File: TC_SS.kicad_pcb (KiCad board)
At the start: 2 copper layers, 106.7 x 124.5 mm, 41 parts, among them Q1 IPW60R099P6XKSA1, Q2 IPW60R099P6XKSA1, Q3 IPW60R099P6XKSA1, Q4 IPW60R099P6XKSA1, U1 IR2184, U2 IR2184, U3 SN74LVC1G14DBV, U4 SN74LVC1G14DBV, U5 NE555D

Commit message: Update Power PCB
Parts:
- added C12: 100n?, Capacitor_SMD:C_2220_5650Metric, F.Cu at (138.5, 121.5)
- added C13: 100n?, Capacitor_SMD:C_2220_5650Metric, F.Cu at (138.5, 114.5)
- added C14: 100n?, Capacitor_SMD:C_2220_5650Metric, F.Cu at (138.5, 107.0)
- added C15: 100n?, Capacitor_SMD:C_2220_5650Metric, F.Cu at (138.5, 99.5)
- added C16: 100n?, Capacitor_SMD:C_2220_5650Metric, F.Cu at (187.5, 121.0)
- added C17: 100n?, Capacitor_SMD:C_2220_5650Metric, F.Cu at (187.5, 114.0)
- added C18: 100n?, Capacitor_SMD:C_2220_5650Metric, F.Cu at (195.0, 109.5)
- added C19: 100n?, Capacitor_SMD:C_2220_5650Metric, F.Cu at (202.0, 109.5)
- added C20: 100n, Capacitor_SMD:C_2220_5650Metric, F.Cu at (177.9, 134.6)
- added C21: 100n, Capacitor_SMD:C_2220_5650Metric, F.Cu at (177.9, 140.5)
- C1, C10, C11: value 100n? -> 100n; footprint Capacitor_SMD:C_2220_5750Metric -> Capacitor_SMD:C_2220_5650Metric
- C3, C4, C5, C6: footprint Capacitor_THT:C_Radial_D8.0mm_H11.5mm_P3.50mm -> Capacitor_THT:CP_Radial_D35.0mm_P10.00mm_SnapIn
- moved FL1 175.0 mm to (17.7, 103.5)
- moved D2 132.2 mm to (48.1, 106.7)
- moved C4 120.1 mm to (28.0, 71.0)
- moved C5 108.7 mm to (28.0, 33.0)
- moved C3 78.6 mm to (67.1, 70.5)
- moved C6 67.5 mm to (67.0, 32.0)
- moved D11 65.2 mm to (166.0, 58.5), turned to 180 degrees
- moved D1 63.6 mm to (129.5, 126.0), turned to 180 degrees
- moved D3 62.6 mm to (210.5, 129.0), turned to 180 degrees
- moved R6 56.1 mm to (208.0, 138.0), turned to -90 degrees
- moved D10 52.7 mm to (152.2, 64.1)
- moved D8 52.7 mm to (152.2, 53.0)
- moved D9 52.7 mm to (152.2, 58.5)
- moved C2 51.6 mm to (132.5, 129.5), turned to 180 degrees
- moved D6 51.6 mm to (202.5, 138.0), turned to 180 degrees
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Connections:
- net Net-(D4-A) renamed /HS1_G
- net Net-(D5-A) renamed /LS1_G
- net Net-(Q1-S) renamed /HB1
- net Net-(Q3-D) renamed /HB2
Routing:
- net /HB1: track 41.8 -> 0.00 mm
- net Net-(D4-K): track 24.3 -> 0.00 mm
- net /HB2: track 27.8 -> 4.50 mm
- net Net-(D5-K): track 22.5 -> 0.00 mm
- net GND: track 21.8 -> 4.77 mm, vias 0 -> 80
- net /HS1_G: track 13.4 -> 0.00 mm
- net /HS2_G: track 3.56 -> 11.5 mm
- net /LS1_G: track 7.64 -> 0.00 mm
- net Net-(D1-K): track 0.00 -> 7.04 mm
- net Net-(D1-A): track 0.00 -> 6.75 mm
- net Net-(D3-A): track 0.00 -> 6.13 mm
- net Net-(D3-K): track 0.00 -> 5.18 mm
- net Net-(U1-VS): track 0.00 -> 4.93 mm
- net Net-(U2-VS): track 0.00 -> 4.54 mm
- net /LS2_G: track 3.72 -> 7.91 mm
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- added copper zone on F.Cu, net /HB1
- added copper zone on F.Cu, net /HB2
- added copper zone on F.Cu, net /HS1_G
- added copper zone on F.Cu, net /LS1_G
- added copper zone on B.Cu, net GND
- added copper zone on F.Cu, net Net-(C1-Pad1)
- added copper zone on F.Cu, net Net-(D4-K)
- added copper zone on F.Cu, net Net-(D5-K)
- added copper zone on F.Cu, net VDC

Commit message: Do power PCB layout
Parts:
- moved R8 67.1 mm to (151.5, 130.0)
- moved C14 17.7 mm to (156.0, 109.5), turned to -90 degrees
- moved C15 14.1 mm to (148.5, 109.5), turned to -90 degrees
- moved R6 9.01 mm to (200.5, 143.0), turned to 90 degrees
- moved C18 7.52 mm to (202.5, 110.0), turned to -90 degrees
- moved C19 6.52 mm to (195.5, 110.0), turned to -90 degrees
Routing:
- net Net-(D7-K): track 13.1 -> 0.00 mm
- net /HS2_G: track 11.5 -> 0.00 mm
- net Net-(D6-K): track 8.49 -> 0.00 mm
- net /LS2_G: track 7.91 -> 0.00 mm
- net Net-(D1-K): track 7.04 -> 0.00 mm
- net Net-(D1-A): track 6.75 -> 0.00 mm
- net Net-(D3-A): track 6.13 -> 0.00 mm
- net Net-(D3-K): track 5.18 -> 0.00 mm
- net Net-(U1-VS): track 4.93 -> 0.00 mm
- net GND: track 4.77 -> 0.00 mm, vias 80 -> 82
- net Net-(U2-VS): track 4.54 -> 0.00 mm
- net /HB2: track 4.50 -> 0.00 mm
- added copper zone on F.Cu, net /HS2_G
- added copper zone on F.Cu, net /LS2_G
- added copper zone on F.Cu, net Net-(D1-A)
- added copper zone on F.Cu, net Net-(D1-K)
- added copper zone on F.Cu, net Net-(D3-A)
- added copper zone on F.Cu, net Net-(D3-K)
- added copper zone on F.Cu, net Net-(D6-K)
- added copper zone on F.Cu, net Net-(D7-K)
- added copper zone on F.Cu, net Net-(U1-VS)
- added copper zone on F.Cu, net Net-(U2-VS)
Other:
- board size 106.7 x 124.5 mm -> 93.2 x 51 mm

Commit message: Update schematic
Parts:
- removed C3, C4, C5, C6: 330u, Capacitor_THT:CP_Radial_D35.0mm_P10.00mm_SnapIn
- removed C8, C9: C, Capacitor_SMD:C_0805_2012Metric_Pad1.18x1.45mm_HandSolder
- removed D10, D11, D8, D9: 1n4148, Diode_SMD:D_SMB
- removed D2: D_Bridge_+-AA, Diode_THT:Diode_Bridge_Vishay_KBPC6
- removed FL1: Filter_EMI_CommonMode, Inductor_THT:L_CommonMode_PulseElectronics_PH9455x155NL_1
- removed U3, U4: SN74LVC1G14DBV, Package_TO_SOT_SMD:SOT-23-5
- removed U5: NE555D, Package_SO:SOIC-8_3.9x4.9mm_P1.27mm
- C12, C13, C14, C15, C16, C17, C18, C19: value 100n? -> 100n

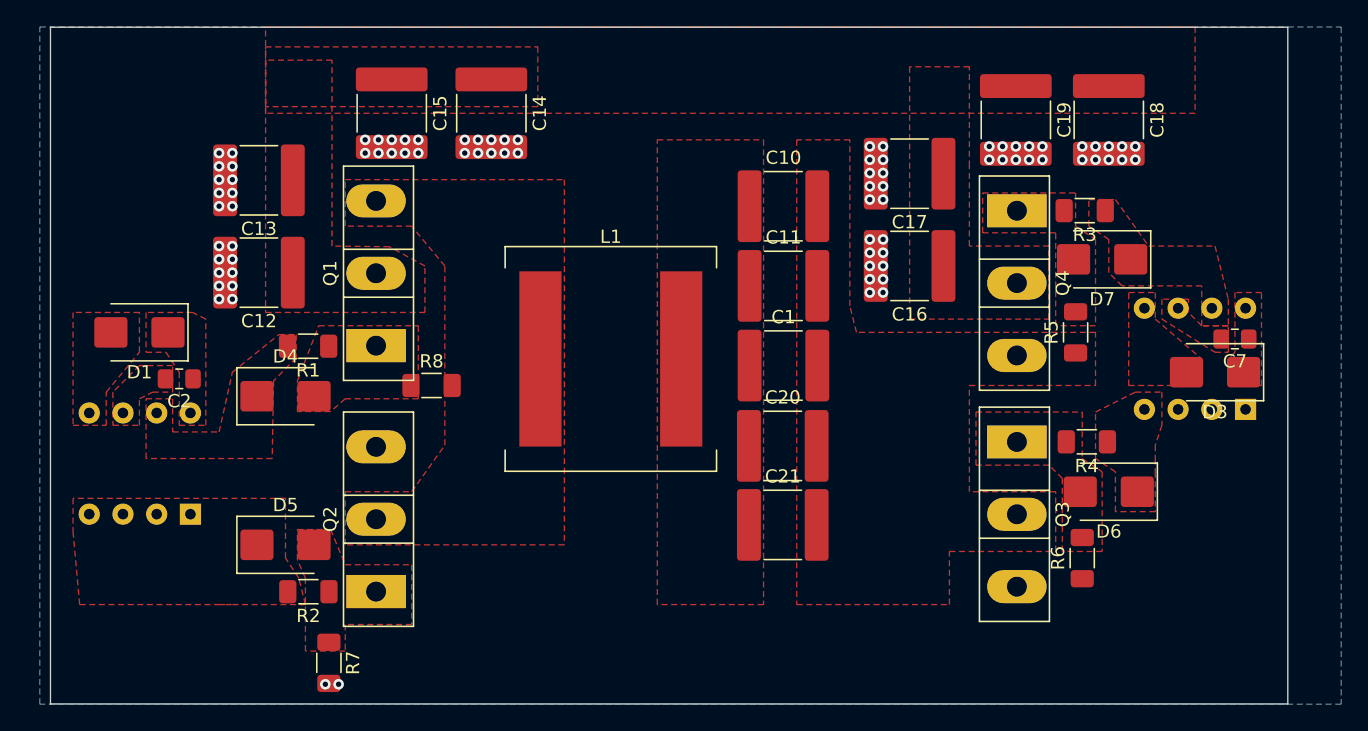
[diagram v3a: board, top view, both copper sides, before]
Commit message: Swap gate driver for Adum4221-1
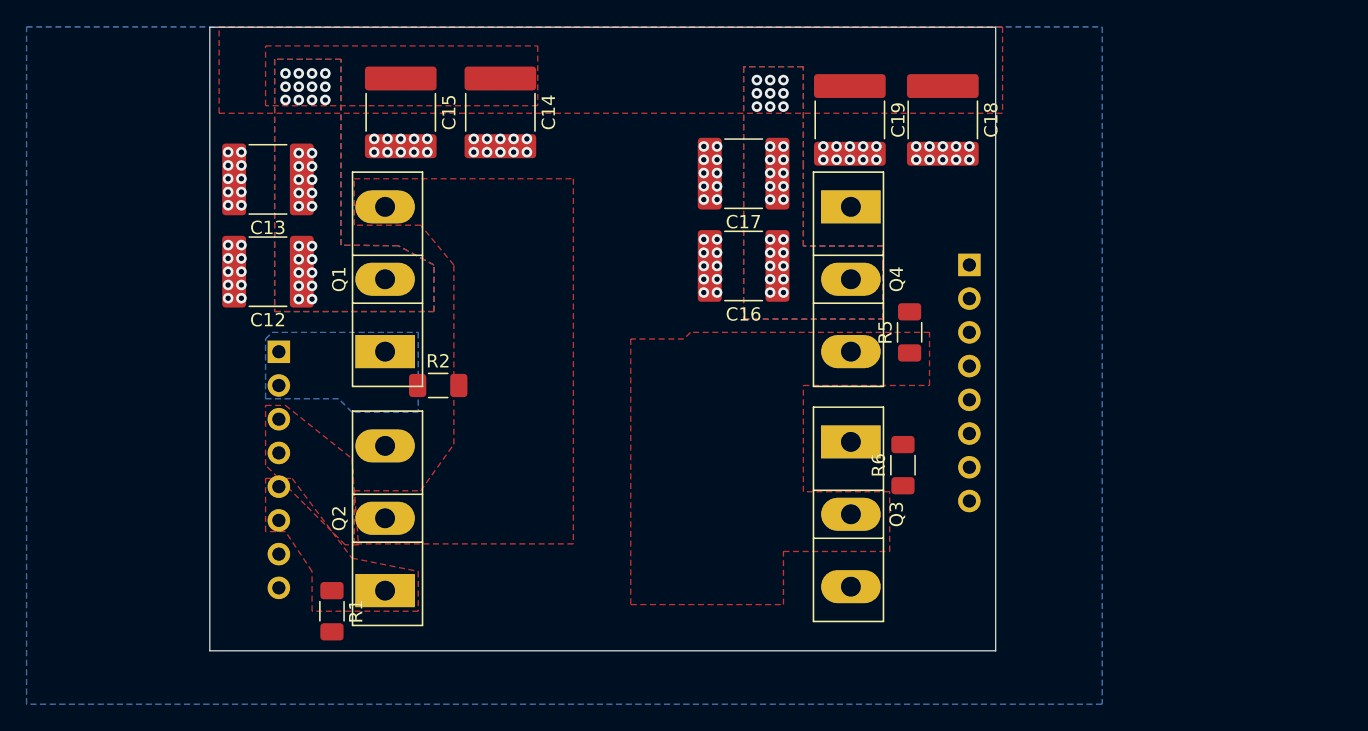
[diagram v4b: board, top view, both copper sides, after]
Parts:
- removed C1, C10, C11, C20, C21: 100n, Capacitor_SMD:C_2220_5650Metric
- removed C2, C7: 100n, Capacitor_SMD:C_0805_2012Metric_Pad1.18x1.45mm_HandSolder
- removed D1, D3: STTH2R06, Diode_SMD:D_SMB
- removed D4, D5, D6, D7: 1n4148, Diode_SMD:D_SMB
- removed L1: ?, Inductor_SMD:L_Coilcraft_XAL1510-472
- removed R3, R4: 22, Resistor_SMD:R_1206_3216Metric_Pad1.30x1.75mm_HandSolder
- removed R7, R8: 10k, Resistor_SMD:R_1206_3216Metric_Pad1.30x1.75mm_HandSolder
- removed U1, U2: IR2184, Package_DIP:DIP-8_W7.62mm_Socket
- added J1: Conn_01x08_Pin, Connector_PinHeader_2.54mm:PinHeader_1x08_P2.54mm_Vertical, B.Cu at (140.0, 127.5)
- added J2: Conn_01x08_Pin, Connector_PinHeader_2.54mm:PinHeader_1x08_P2.54mm_Vertical, B.Cu at (192.0, 120.9)
- R1, R2: value 22 -> 10k
- moved R1 20.0 mm to (144.0, 147.0), turned to -90 degrees
- moved R2 18.4 mm to (152.0, 130.0), turned to 0 degrees
- moved R6 15.2 mm to (187.0, 136.0)
- moved Q4 12.5 mm to (183.1, 116.5)
- moved C16 12.5 mm to (175.0, 121.0)
- moved C17 12.5 mm to (175.0, 114.0)
- moved C18 12.5 mm to (190.0, 110.0)
- moved C19 12.5 mm to (183.0, 110.0)
- moved Q3 12.5 mm to (183.1, 134.2)
- moved R5 12.5 mm to (187.5, 126.0)
- moved Q1 0.82 mm to (148.0, 127.5)
- moved Q2 0.68 mm to (148.0, 145.4)
- moved C12 0.68 mm to (139.2, 121.4)
- moved C13 0.68 mm to (139.2, 114.5)
- moved C14 0.68 mm to (156.7, 109.4)
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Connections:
- net /HS2_G renamed Net-(J2-Pin_7)
- net /LS2_G renamed Net-(J2-Pin_3)
- R1 pad 1: /HS1_G -> /LS1_G
- R1 pad 2: Net-(D4-K) -> GND
- R2 pad 1: /LS1_G -> /HS1_G
- R2 pad 2: Net-(D5-K) -> /HB1
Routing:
- net VDC: vias 0 -> 61
- net GND: vias 82 -> 80
- added copper zone on B.Cu, net /HS1_G
- added copper zone on B.Cu, net VDC
- removed copper zone on F.Cu, net /HS1_G
- removed copper zone on F.Cu, net Net-(C1-Pad1)
- removed copper zone on F.Cu, net Net-(D1-A)
- removed copper zone on F.Cu, net Net-(D1-K)
- removed copper zone on F.Cu, net Net-(D3-A)
- removed copper zone on F.Cu, net Net-(D3-K)
- removed copper zone on F.Cu, net Net-(D4-K)
- removed copper zone on F.Cu, net Net-(D5-K)
- removed copper zone on F.Cu, net Net-(D6-K)
- removed copper zone on F.Cu, net Net-(D7-K)
- removed copper zone on F.Cu, net Net-(J2-Pin_3)
- removed copper zone on F.Cu, net Net-(J2-Pin_7)
- removed copper zone on F.Cu, net Net-(U1-VS)
- removed copper zone on F.Cu, net Net-(U2-VS)
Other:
- board size 93.2 x 51 mm -> 59.2 x 47 mm

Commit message: Update basically everything
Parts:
- removed J2: Conn_01x08_Pin, Connector_PinHeader_2.54mm:PinHeader_1x08_P2.54mm_Vertical
- added C1: 1u, Capacitor_SMD:C_0805_2012Metric, F.Cu at (202.7, 120.7)
- added C2: 1u, Capacitor_SMD:C_0805_2012Metric, F.Cu at (202.7, 117.7)
- added C3: 100n, Capacitor_SMD:C_2220_5650Metric, F.Cu at (114.5, 133.1)
- added C4: 1u, Capacitor_SMD:C_0805_2012Metric, F.Cu at (112.5, 107.1)
- added C5: 1u, Capacitor_SMD:C_0805_2012Metric, F.Cu at (112.5, 110.1)
- added C6: 1u, Capacitor_SMD:C_0805_2012Metric, F.Cu at (112.5, 113.1)
- added C7: 1u, Capacitor_SMD:C_0805_2012Metric, F.Cu at (112.5, 116.1)
- added C8: 1u, Capacitor_SMD:C_0805_2012Metric, F.Cu at (112.5, 119.2)
- added C9: 1u, Capacitor_SMD:C_0805_2012Metric, F.Cu at (112.5, 122.2)
- added D1: D, PCM_Diode_SMD_AKL:D_PowerDI-123, F.Cu at (188.5, 136.0)
- added D2: 1N4148WT, Diode_SMD:D_SOD-523, F.Cu at (116.5, 106.8)
- added D3: 1N4148WT, Diode_SMD:D_SOD-523, F.Cu at (116.5, 109.3)
- added D4: D, PCM_Diode_SMD_AKL:D_PowerDI-123, F.Cu at (211.5, 138.4)
- added D5: D, PCM_Diode_SMD_AKL:D_PowerDI-123, F.Cu at (211.5, 142.7)
- added D6: D, PCM_Diode_SMD_AKL:D_PowerDI-123, F.Cu at (211.5, 147.0)
- added IC1: ADUM4221-1ARIZ, SamacSys_Parts:SOIC127P1030X264-16N, F.Cu at (137.0, 134.0)
- added IC2: ADUM4221-1ARIZ, SamacSys_Parts:SOIC127P1030X264-16N, F.Cu at (195.5, 127.5)
- added PS1: RKZ-1215S_H, symbol:RKZ1215SH, B.Cu at (125.0, 108.3)
- added PS2: RKZ-1215S_H, symbol:RKZ1215SH, B.Cu at (123.2, 134.2)
- added PS3: RKZ-1215S_H, symbol:RKZ1215SH, B.Cu at (195.2, 153.2)
- added PS4: RKZ-1215S_H, symbol:RKZ1215SH, B.Cu at (213.5, 104.5)
- added R10: 100, Resistor_SMD:R_0805_2012Metric, F.Cu at (117.1, 138.1)
- added R11: 4.7, Resistor_SMD:R_0805_2012Metric, F.Cu at (117.1, 141.0)
- added R3: 10k, Resistor_SMD:R_0805_2012Metric, F.Cu at (207.1, 132.3)
- added R4: 10k, Resistor_SMD:R_0805_2012Metric, F.Cu at (207.1, 129.4)
- added R7: 22, Resistor_SMD:R_0805_2012Metric, F.Cu at (187.5, 133.5)
- added R8: 22, Resistor_SMD:R_0805_2012Metric, F.Cu at (207.1, 117.6)
- added R9: 4.7, Resistor_SMD:R_0805_2012Metric, F.Cu at (207.1, 114.6)
- added U1: LM7805_TO220, Package_TO_SOT_THT:TO-220-3_Vertical, F.Cu at (113.5, 127.6)
- J1: value Conn_01x08_Pin -> 12V_In; footprint Connector_PinHeader_2.54mm:PinHeader_1x08_P2.54mm_Vertical -> Connector_PinHeader_2.54mm:PinHeader_1x02_P2.54mm_Vertical; moved to F.Cu
- R1, R2, R5, R6: footprint Resistor_SMD:R_1206_3216Metric_Pad1.30x1.75mm_HandSolder -> Resistor_SMD:R_0805_2012Metric
- moved J1 29.7 mm to (112.6, 138.9), turned to 0 degrees
- moved R5 19.6 mm to (207.1, 126.4), turned to 180 degrees
- moved R6 17.0 mm to (202.5, 143.0), turned to 180 degrees
- moved C12 2.81 mm to (136.4, 121.4)
- moved C13 2.81 mm to (136.4, 114.5)
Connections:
- J1 pad 1: /HS1_G -> GND
- J1 pad 2: /HS1_G -> +12V
- Q1 pad 3: /HB1 -> HB1
- Q2 pad 2: /HB1 -> HB1
- Q3 pad 1: Net-(J2-Pin_3) -> Net-(D1-A)
- Q3 pad 2: /HB2 -> HB2
- Q4 pad 1: Net-(J2-Pin_7) -> Net-(D4-A)
- Q4 pad 3: /HB2 -> HB2
- R2 pad 2: /HB1 -> HB1
- R5 pad 1: /HB2 -> Net-(D6-A)
- R5 pad 2: Net-(J2-Pin_7) -> /HS1_G
- R6 pad 1: GND -> Net-(D5-A)
- R6 pad 2: Net-(J2-Pin_3) -> /LS1_G
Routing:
- net GND: vias 80 -> 81
- added copper zone on F.Cu, net HB1
- added copper zone on F.Cu, net HB2
- removed copper zone on F.Cu, net /HB1
- removed copper zone on F.Cu, net /HB2
- removed copper zone on F.Cu, net /LS1_G
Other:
- board size 59.2 x 47 mm -> 106.7 x 58 mm

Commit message: Almost ready to produce
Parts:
- added C10: 10u, Capacitor_SMD:C_0805_2012Metric, F.Cu at (115.4, 108.1)
- added C11: 1u, Capacitor_SMD:C_0805_2012Metric, F.Cu at (119.4, 108.1)
- added C20: 1u, Capacitor_SMD:C_0805_2012Metric, F.Cu at (137.2, 147.5)
- added C21: 1u, Capacitor_SMD:C_0805_2012Metric, F.Cu at (133.8, 147.5)
- added C22: 1u, Capacitor_SMD:C_0805_2012Metric, B.Cu at (136.8, 132.5)
- added C23: 1u, Capacitor_SMD:C_0805_2012Metric, B.Cu at (133.2, 132.5)
- added C24: 100n, Capacitor_SMD:C_0805_2012Metric, F.Cu at (137.0, 145.5)
- added C25: 100n, Capacitor_SMD:C_0805_2012Metric, F.Cu at (133.8, 145.5)
- added C26: 100n, Capacitor_SMD:C_0805_2012Metric, B.Cu at (133.2, 134.5)
- added C27: 100n, Capacitor_SMD:C_0805_2012Metric, B.Cu at (136.8, 134.5)
- added C28: 1u, Capacitor_SMD:C_0805_2012Metric, F.Cu at (189.6, 159.7)
- added C29: 1u, Capacitor_SMD:C_0805_2012Metric, F.Cu at (189.6, 162.8)
- added C30: 1u, Capacitor_SMD:C_0805_2012Metric, F.Cu at (195.0, 116.0)
- added C31: 1u, Capacitor_SMD:C_0805_2012Metric, F.Cu at (194.1, 153.7)
- added C32: 1u, Capacitor_SMD:C_0805_2012Metric, F.Cu at (194.1, 156.7)
- added C33: 1u, Capacitor_SMD:C_0805_2012Metric, F.Cu at (194.1, 159.7)
- added C34: 100n, Capacitor_SMD:C_0805_2012Metric, F.Cu at (194.1, 162.8)
- added C35: 100n, Capacitor_SMD:C_0805_2012Metric, F.Cu at (198.5, 150.7)
- added C36: 1u, Capacitor_SMD:C_0805_2012Metric, F.Cu at (198.5, 153.7)
- added C37: 1u, Capacitor_SMD:C_0805_2012Metric, F.Cu at (123.2, 147.5)
- added C38: 1u, Capacitor_SMD:C_0805_2012Metric, F.Cu at (123.0, 127.5)
- added C39: 1u, Capacitor_SMD:C_0805_2012Metric, F.Cu at (198.5, 162.8)
- added H1: MountingHole_Pad, MountingHole:MountingHole_3.2mm_M3_Pad_Via, F.Cu at (114.8, 157.5)
- added H2: MountingHole_Pad, MountingHole:MountingHole_3.2mm_M3_Pad_Via, F.Cu at (114.2, 117.0)
- added H3: MountingHole_Pad, MountingHole:MountingHole_3.2mm_M3_Pad_Via, F.Cu at (204.8, 105.2)
- added H4: MountingHole_Pad, MountingHole:MountingHole_3.2mm_M3_Pad_Via, F.Cu at (121.8, 157.5)
- added J2: Conn_Coaxial, Connector_Coaxial:SMA_Samtec_SMA-J-P-X-ST-EM1_EdgeMount, F.Cu at (85.4, 109.7)
- added J3: Conn_Coaxial, Connector_Coaxial:SMA_Samtec_SMA-J-P-X-ST-EM1_EdgeMount, F.Cu at (112.7, 133.2)
- added J4: Conn_Coaxial, Connector_Coaxial:SMA_Samtec_SMA-J-P-X-ST-EM1_EdgeMount, F.Cu at (112.7, 142.8)
- added J5: Conn_Coaxial, Connector_Coaxial:SMA_Samtec_SMA-J-P-X-ST-EM1_EdgeMount, F.Cu at (221.8, 124.8)
- added J6: Conn_Coaxial, Connector_Coaxial:SMA_Samtec_SMA-J-P-X-ST-EM1_EdgeMount, F.Cu at (221.6, 139.2)
- added TP1: TestPoint, TestPoint:TestPoint_Loop_D3.50mm_Drill1.4mm_Beaded, F.Cu at (83.3, 119.7)
- added TP2: TestPoint, TestPoint:TestPoint_Loop_D3.50mm_Drill1.4mm_Beaded, F.Cu at (102.8, 119.4)
- added U2: 74HC14, SamacSys_Parts:SOIC127P600X175-14N, F.Cu at (93.0, 109.7)
- added U3: LM7812_TO220, Package_TO_SOT_THT:TO-220-3_Vertical, F.Cu at (114.8, 104.1)
- C4: value 1u -> 10u
- C8, C9: moved to B.Cu
- D1, D4, D5, D6: value D -> DFLS120L-7
- J1: value 12V_In -> 15V_In
- R5, R6: value 10k -> 22
- moved C8 89.3 mm to (201.0, 130.8), turned to 180 degrees
- moved C9 88.3 mm to (200.8, 124.5), turned to 180 degrees
- moved R11 88.2 mm to (204.5, 129.2), turned to 90 degrees
- moved R9 83.5 mm to (127.2, 139.0), turned to -90 degrees
- moved D6 70.5 mm to (143.0, 130.2)
- moved D5 68.0 mm to (143.5, 143.5)
- moved R5 63.6 mm to (143.5, 127.8), turned to 0 degrees
- moved R6 58.8 mm to (143.8, 145.8), turned to 0 degrees
- moved PS3 36.3 mm to (209.7, 120.0)
- moved PS4 33.9 mm to (209.8, 138.2)
- moved J1 27.6 mm to (111.9, 111.3), turned to 180 degrees
- moved D3 27.4 mm to (89.8, 115.4), turned to 180 degrees
- moved U1 27.0 mm to (127.0, 104.2)
- moved R10 26.9 mm to (96.8, 120.4), turned to 90 degrees
- moved C3 26.2 mm to (92.1, 119.4)
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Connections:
- D3 pad 2: Net-(D3-A) -> GND
- D5 pad 1: /LS1_G -> Net-(D5-K)
- D5 pad 2: Net-(D5-A) -> /LS1_G
- D6 pad 1: /HS1_G -> Net-(D6-K)
- D6 pad 2: Net-(D6-A) -> /HS1_G
- IC1 pad 1: PWM -> Net-(IC1-PWM)
- IC1 pad 10: Net-(D5-A) -> Net-(D5-K)
- IC1 pad 15: Net-(D6-A) -> Net-(D6-K)
- IC1 pad 5: unconnected-(IC1-DISABLE-Pad5) -> Net-(IC1-DISABLE)
- IC2 pad 1: PWM -> Net-(IC2-PWM)
- IC2 pad 5: unconnected-(IC2-DISABLE-Pad5) -> Net-(IC2-DISABLE)
- J1 pad 2: +12V -> Net-(J1-Pin_2)
- PS3 pad 1: unconnected-(PS3-+VIN-Pad1) -> +12V
- PS3 pad 2: unconnected-(PS3--VIN-Pad2) -> GND
- PS3 pad 5: unconnected-(PS3--VOUT-Pad5) -> Vg_neg_HS2
- PS3 pad 6: unconnected-(PS3-NO_PIN-Pad6) -> HB2
- PS3 pad 7: unconnected-(PS3-+VOUT-Pad7) -> Vg_pos_HS2
- R5 pad 1: Net-(D6-A) -> Net-(D6-K)
- R6 pad 1: Net-(D5-A) -> Net-(D5-K)
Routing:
- net GND: track 0.00 -> 41.4 mm
- net HB1: track 0.00 -> 33.2 mm
- net +5V: track 0.00 -> 26.7 mm, vias 0 -> 2
- net Net-(IC1-DISABLE): track 0.00 -> 19.2 mm
- net Net-(IC1-PWM): track 0.00 -> 17.9 mm
- net /LS1_G: track 0.00 -> 13.6 mm
- net Vg_neg_HS1: track 0.00 -> 12.6 mm, vias 0 -> 2
- net Vg_neg_LS1: track 0.00 -> 12.6 mm
- net Vg_pos_LS1: track 0.00 -> 11.1 mm, vias 0 -> 3
- net /HS1_G: track 0.00 -> 10.1 mm
- net Net-(D6-K): track 0.00 -> 9.86 mm
- net Net-(D2-A): track 0.00 -> 9.44 mm
- net +12V: track 0.00 -> 9.33 mm
- net Net-(#T1-SB): track 0.00 -> 6.99 mm
- net Net-(J1-Pin_2): track 0.00 -> 6.98 mm
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- added copper zone on F.Cu, net /LS1_G
- added copper zone on F.Cu, net GND
- added copper zone on F.Cu, net Net-(D1-A)
- removed copper zone on B.Cu, net /HS1_G
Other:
- board size 106.7 x 58 mm -> 113.8 x 64.3 mm

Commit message: Done now (probably)
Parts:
- C30, C31: value 1u -> 100n; moved to B.Cu
- C32, C33, C34, C35, R11, R4: moved to B.Cu
- moved TP1 134.1 mm to (210.2, 162.8), turned to 180 degrees
- moved J2 126.5 mm to (200.1, 163.0), turned to 0 degrees
- moved D3 123.8 mm to (205.8, 158.7), turned to -90 degrees
- moved C3 123.3 mm to (209.8, 156.3), turned to 90 degrees
- moved D2 121.3 mm to (205.8, 156.7), turned to -90 degrees
- moved R10 118.1 mm to (210.8, 151.6), turned to 180 degrees
- moved U2 116.5 mm to (200.1, 155.4), turned to 180 degrees
- moved C6 115.9 mm to (204.8, 152.9), turned to 90 degrees
- moved TP2 112.8 mm to (211.8, 148.2), turned to 180 degrees
- moved C7 109.2 mm to (195.3, 151.7), turned to 90 degrees
- moved H4 98.7 mm to (220.4, 161.6)
- moved C39 45.6 mm to (208.5, 118.2)
- moved C29 42.0 mm to (198.8, 121.8)
- moved C28 38.4 mm to (195.2, 121.8)
- moved R8 34.0 mm to (188.5, 118.8), turned to 0 degrees
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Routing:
- net +12V: track 9.33 -> 183.6 mm, vias 0 -> 2
- net +5V: track 26.7 -> 185.5 mm, vias 2 -> 7
- net HB2: track 0.00 -> 37.0 mm
- net Net-(IC2-DISABLE): track 0.00 -> 22.5 mm
- net Net-(IC2-PWM): track 0.00 -> 21.1 mm
- net Vg_neg_HS2: track 0.00 -> 17.3 mm, vias 0 -> 3
- net Net-(D1-A): track 0.00 -> 14.1 mm
- net Vg_neg_LS2: track 0.00 -> 13.3 mm, vias 0 -> 2
- net Net-(D4-K): track 0.00 -> 11.7 mm
- net Net-(D4-A): track 0.00 -> 11.1 mm, vias 0 -> 1
- net PWM: track 0.00 -> 9.68 mm
- net Vg_pos_HS2: track 0.00 -> 9.39 mm, vias 0 -> 3
- net GND: track 41.4 -> 49.8 mm, vias 81 -> 402
- net Net-(D1-K): track 0.00 -> 7.52 mm
- net Vg_pos_LS2: track 0.00 -> 6.09 mm, vias 0 -> 1
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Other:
- outline, holes or cut-outs redrawn
- board text added: "+325VDC"
- board text added: "Disable"
- board text added: "PPFE Tesla Coil Driver V.1"
- board text added: "PWM"
